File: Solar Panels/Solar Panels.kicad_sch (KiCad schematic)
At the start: 54 parts, among them J2 5040500891

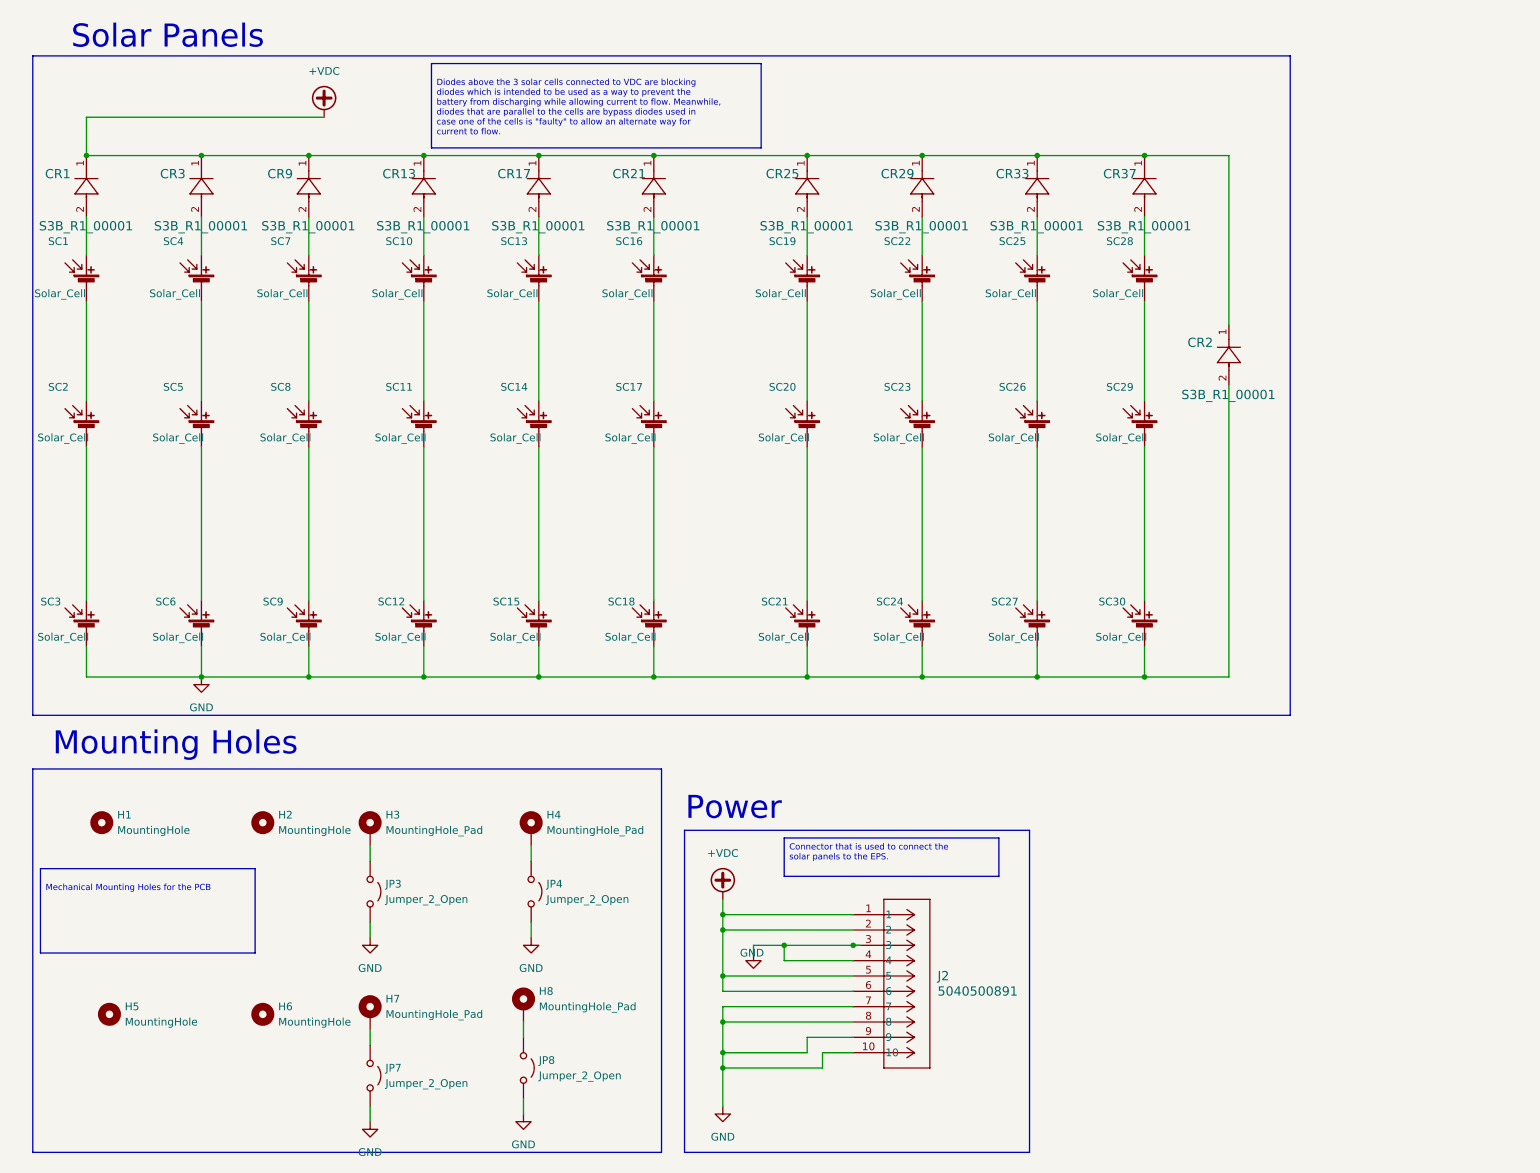
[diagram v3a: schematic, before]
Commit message: Routed the PCB after the Footprint Adjustments
Routed the PCB after making adjustments to the TriSolX footprint.
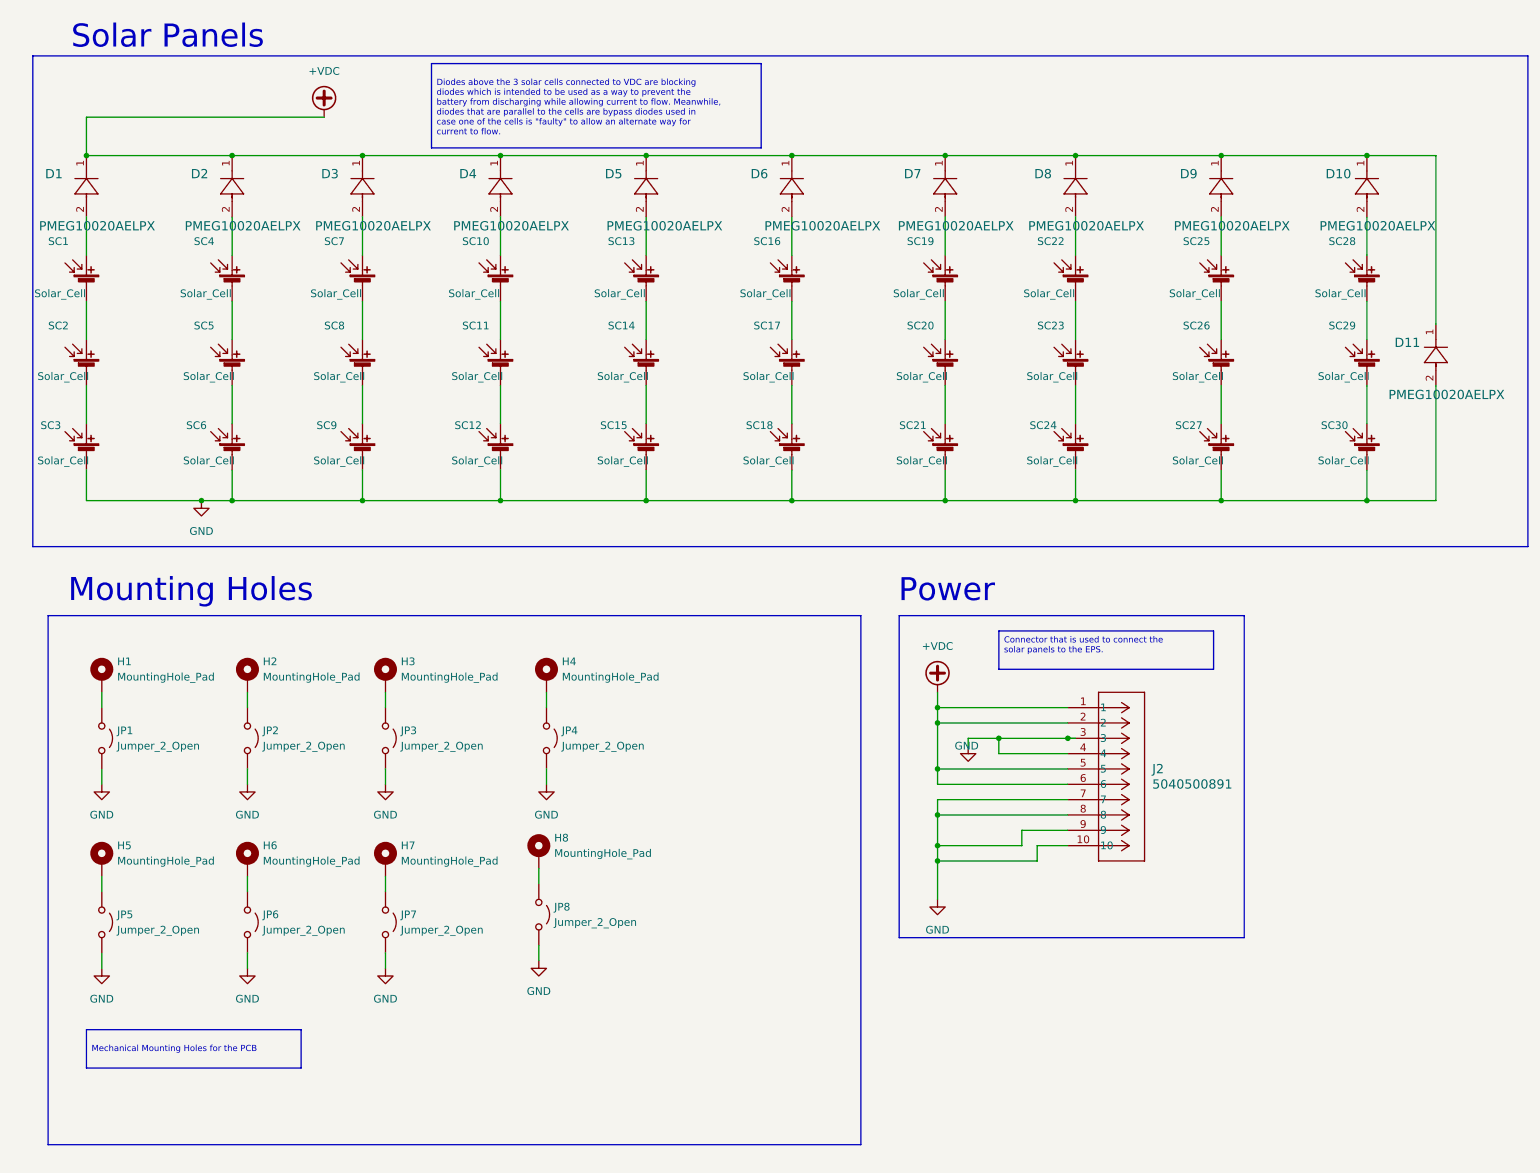
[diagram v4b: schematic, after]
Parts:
- removed H1, H2, H5, H6: MountingHole, MountingHole:MountingHole_3.2mm_M3_DIN965_Pad, symbol Mechanical:MountingHole
- added H1, H2, H5, H6: MountingHole_Pad, MountingHole:MountingHole_3.2mm_M3_DIN965_Pad, symbol Mechanical:MountingHole_Pad
- added JP1, JP2, JP5, JP6: Jumper_2_Open, Jumper:SolderJumper-2_P1.3mm_Open_Pad1.0x1.5mm, symbol Jumper:Jumper_2_Open
- D1: renamed from CR1; value S3B_R1_00001 -> PMEG10020AELPX; footprint Solar Panel Library:SMC&slash_DO-214AB_PNJ -> Solar Panel Library:PMEG10020AELPX
- D10: renamed from CR37; value S3B_R1_00001 -> PMEG10020AELPX; footprint Solar Panel Library:SMC&slash_DO-214AB_PNJ -> Solar Panel Library:PMEG10020AELPX
- D11: renamed from CR2; value S3B_R1_00001 -> PMEG10020AELPX; footprint Solar Panel Library:SMC&slash_DO-214AB_PNJ -> Solar Panel Library:PMEG10020AELPX
- D2: renamed from CR3; value S3B_R1_00001 -> PMEG10020AELPX; footprint Solar Panel Library:SMC&slash_DO-214AB_PNJ -> Solar Panel Library:PMEG10020AELPX
- D3: renamed from CR9; value S3B_R1_00001 -> PMEG10020AELPX; footprint Solar Panel Library:SMC&slash_DO-214AB_PNJ -> Solar Panel Library:PMEG10020AELPX
- D4: renamed from CR13; value S3B_R1_00001 -> PMEG10020AELPX; footprint Solar Panel Library:SMC&slash_DO-214AB_PNJ -> Solar Panel Library:PMEG10020AELPX
- D5: renamed from CR17; value S3B_R1_00001 -> PMEG10020AELPX; footprint Solar Panel Library:SMC&slash_DO-214AB_PNJ -> Solar Panel Library:PMEG10020AELPX
- D6: renamed from CR21; value S3B_R1_00001 -> PMEG10020AELPX; footprint Solar Panel Library:SMC&slash_DO-214AB_PNJ -> Solar Panel Library:PMEG10020AELPX
- D7: renamed from CR25; value S3B_R1_00001 -> PMEG10020AELPX; footprint Solar Panel Library:SMC&slash_DO-214AB_PNJ -> Solar Panel Library:PMEG10020AELPX
- D8: renamed from CR29; value S3B_R1_00001 -> PMEG10020AELPX; footprint Solar Panel Library:SMC&slash_DO-214AB_PNJ -> Solar Panel Library:PMEG10020AELPX
- D9: renamed from CR33; value S3B_R1_00001 -> PMEG10020AELPX; footprint Solar Panel Library:SMC&slash_DO-214AB_PNJ -> Solar Panel Library:PMEG10020AELPX
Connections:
- net GND: now also JP1.2 (B), JP2.2 (B), JP5.2 (B), JP6.2 (B)
- new net: H1.1, JP1.1 (A)
- new net: H6.1, JP6.1 (A)
- new net: H5.1, JP5.1 (A)
- new net: H2.1, JP2.1 (A)
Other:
- moved on the sheet: D10, D11, D2, D3, D4, D5, D6, D7, D8, D9, H3, H4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
